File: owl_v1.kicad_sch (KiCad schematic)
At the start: 17 parts, among them SW1 SW_SPDT, U1 STM32F103C8T6, Y1 8MHz, Y2 32k768

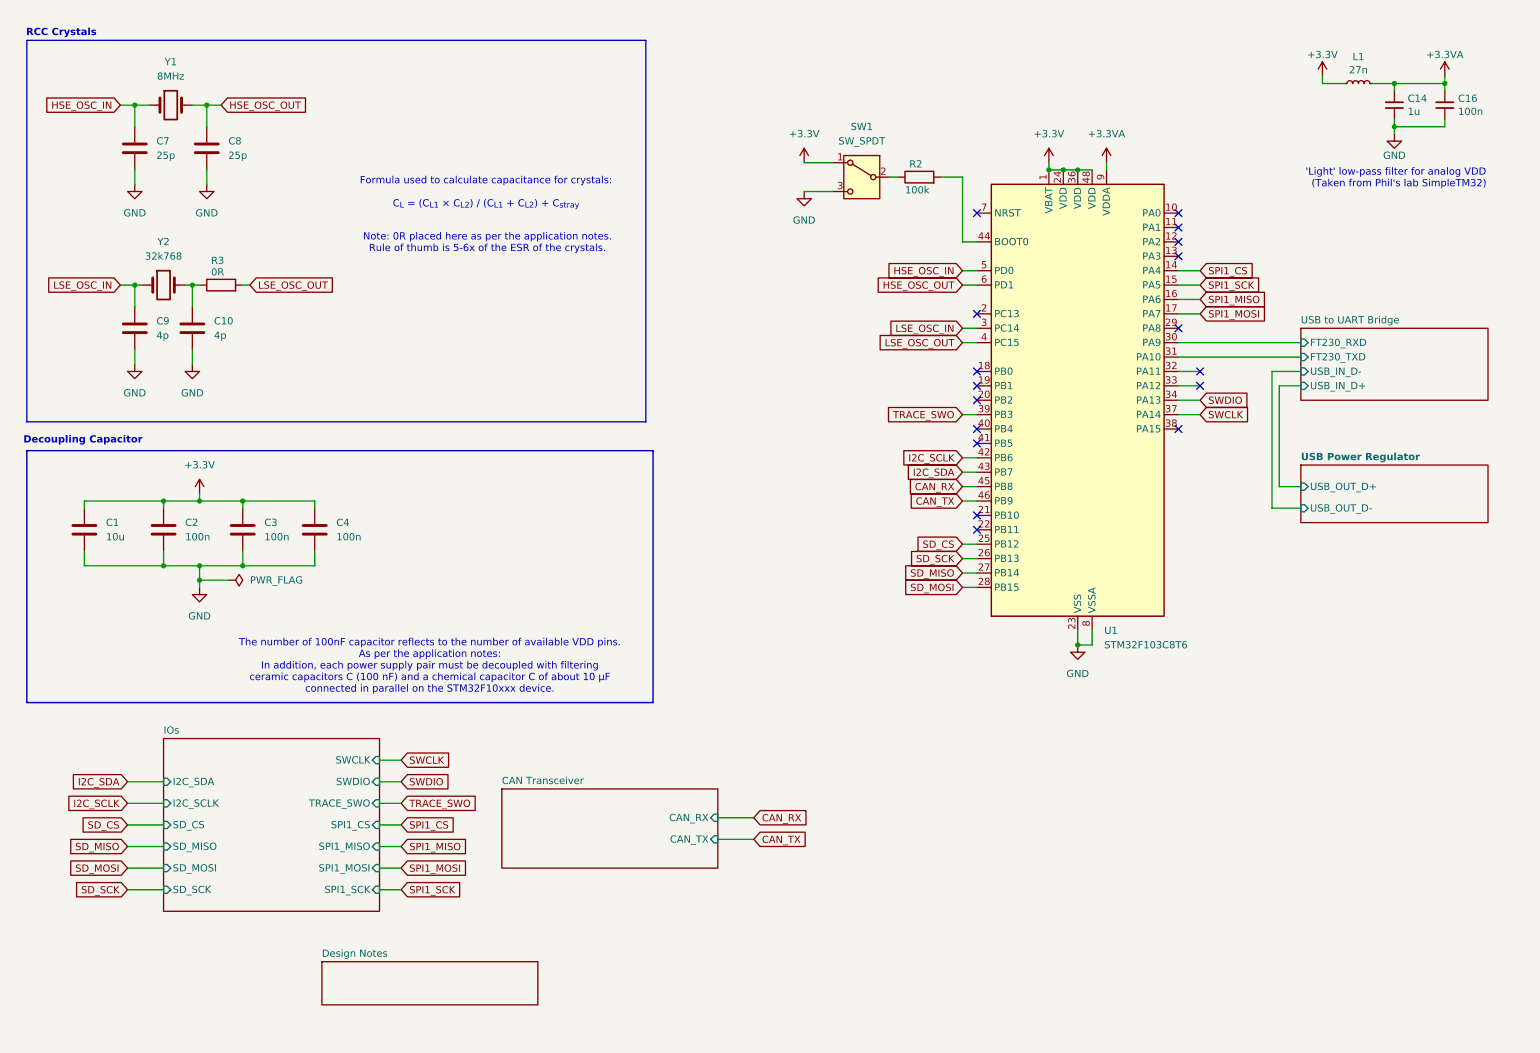
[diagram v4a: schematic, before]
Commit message: [feat] Add OLED I2C breakout for display, Add general purpose GPIOs
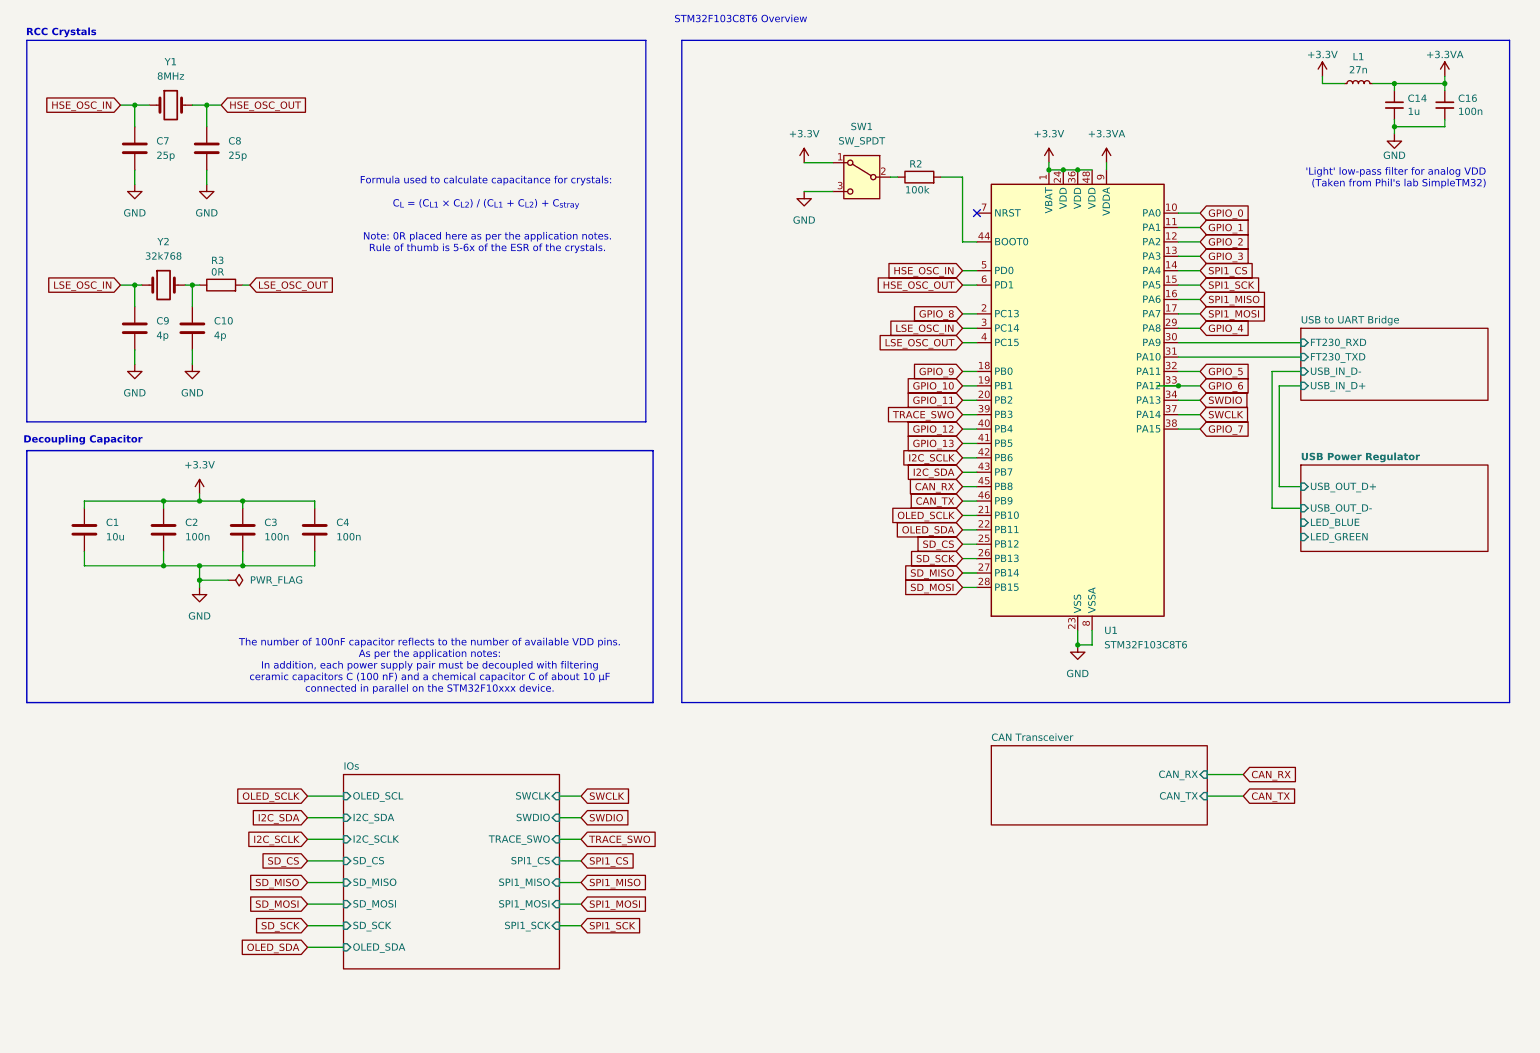
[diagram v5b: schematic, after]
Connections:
- net GPIO_0: now reaches U1.10 (PA0)
- net GPIO_1: now reaches U1.11 (PA1)
- net GPIO_2: now reaches U1.12 (PA2)
- net GPIO_3: now reaches U1.13 (PA3)
- net GPIO_9: now reaches U1.18 (PB0)
- net GPIO_10: now reaches U1.19 (PB1)
- net GPIO_8: now reaches U1.2 (PC13)
- net GPIO_11: now reaches U1.20 (PB2)
- net OLED_SCLK: now reaches U1.21 (PB10)
- net OLED_SDA: now reaches U1.22 (PB11)
- net GPIO_4: now reaches U1.29 (PA8)
- net GPIO_5: now reaches U1.32 (PA11)
- net GPIO_6: now reaches U1.33 (PA12)
- net GPIO_7: now reaches U1.38 (PA15)
- net GPIO_12: now reaches U1.40 (PB4)
- net GPIO_13: now reaches U1.41 (PB5)
- no-connect marks 17 -> 1
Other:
- removed sheet Design Notes
- sheet IOs ports: added OLED_SCL, OLED_SDA; removed none
- sheet USB Power Regulator ports: added LED_BLUE, LED_GREEN; removed none
- note added: "STM32F103C8T6 Overview"

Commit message: [feat] Add footprints for external GPIOs
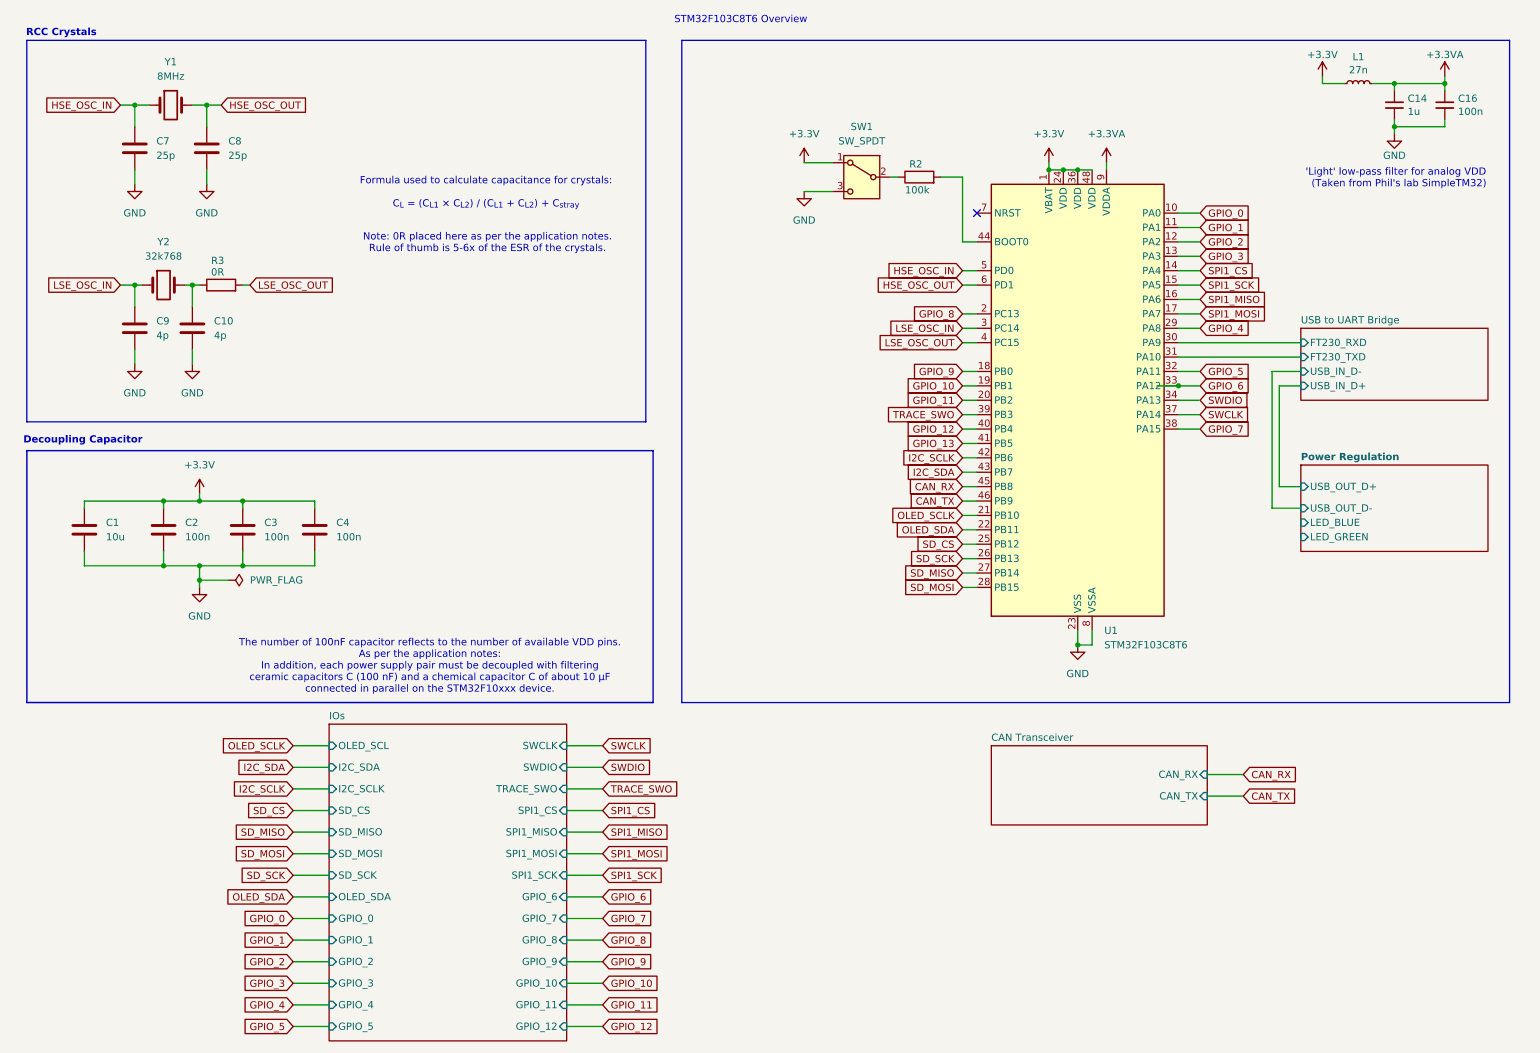
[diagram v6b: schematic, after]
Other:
- sheet USB Power Regulator renamed Power Regulation
- sheet IOs ports: added GPIO_0, GPIO_1, GPIO_10, GPIO_11, GPIO_12, GPIO_2, GPIO_3, GPIO_4, GPIO_5, GPIO_6, GPIO_7, GPIO_8, GPIO_9; removed none

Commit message: [refactor] Remove GPIO12 and GPIO13 for LED green and blue
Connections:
- net GPIO_12 renamed LED_BLUE
- net GPIO_13 renamed LED_GREEN
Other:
- sheet IOs ports: added none; removed GPIO_12
- moved on the sheet: C14, C16, L1

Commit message: [feat] Integrate external battery
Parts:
- C1: value 10u -> 10uF
- C10, C9: value 4p -> 4pF
- C14: value 1u -> 1uF
- C16, C2, C3, C4: value 100n -> 100nF
- C7, C8: value 25p -> 25pF
- L1: value 27n -> 27nH
- R2: value 100k -> 100kR
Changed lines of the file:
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@@
 			)
 		)
-		(property "Value" "10u"
+		(property "Value" "10uF"
 			(at 31.75 107.9499 0)
 			(show_name no)
@@
 			)
 		)
-		(property "Value" "25p"
+		(property "Value" "25pF"
 			(at 53.34 40.6399 0)
 			(show_name no)
@@
 			)
 		)
-		(property "Value" "100n"
+		(property "Value" "100nF"
 			(at 72.39 107.9499 0)
 			(show_name no)
@@
 			)
 		)
-		(property "Value" "4p"
+		(property "Value" "4pF"
 			(at 40.64 72.3899 0)
 			(show_name no)
@@
 			)
 		)
-		(property "Value" "1u"
+		(property "Value" "1uF"
 			(at 256.3368 36.703 0)
 			(show_name no)
@@
 			)
 		)
-		(property "Value" "25p"
+		(property "Value" "25pF"
 			(at 40.64 40.6399 0)
 			(show_name no)
@@
 			)
 		)
-		(property "Value" "100n"
+		(property "Value" "100nF"
 			(at 45.72 107.9499 0)
 			(show_name no)
@@
 			)
 		)
-		(property "Value" "100n"
+		(property "Value" "100nF"
 			(at 59.69 107.9499 0)
 			(show_name no)
@@
 			)
 		)
-		(property "Value" "27n"
+		(property "Value" "27nH"
 			(at 247.65 29.3624 90)
 			(show_name no)
@@
 			)
 		)
-		(property "Value" "100k"
+		(property "Value" "100kR"
 			(at 172.72 46.736 90)
 			(show_name no)
@@
 			)
 		)
-		(property "Value" "4p"
+		(property "Value" "4pF"
 			(at 50.8 72.3899 0)
 			(show_name no)
@@
 			)
 		)
-		(property "Value" "100n"
+		(property "Value" "100nF"
 			(at 265.2268 36.703 0)
 			(show_name no)
@@
 			(project "owl_v1"
 				(path "/c1d8d3e2-84ea-437a-bbb1-a2e651deb7ac"
-					(page "6")
-				)
-			)
+					(page "5")
+				)
+			)
